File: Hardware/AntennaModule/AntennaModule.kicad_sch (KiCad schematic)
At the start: 0 parts

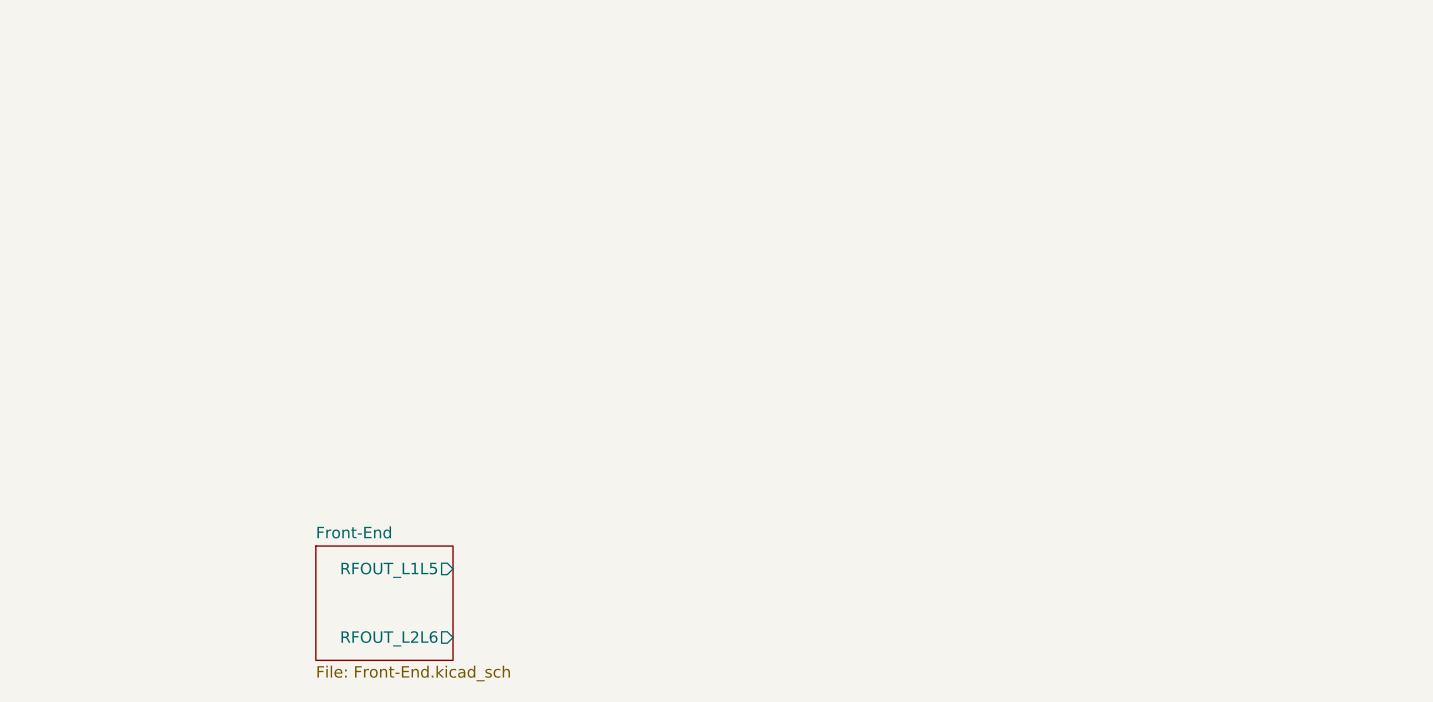
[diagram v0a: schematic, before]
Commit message: TE0149AをTE0133Bに変更
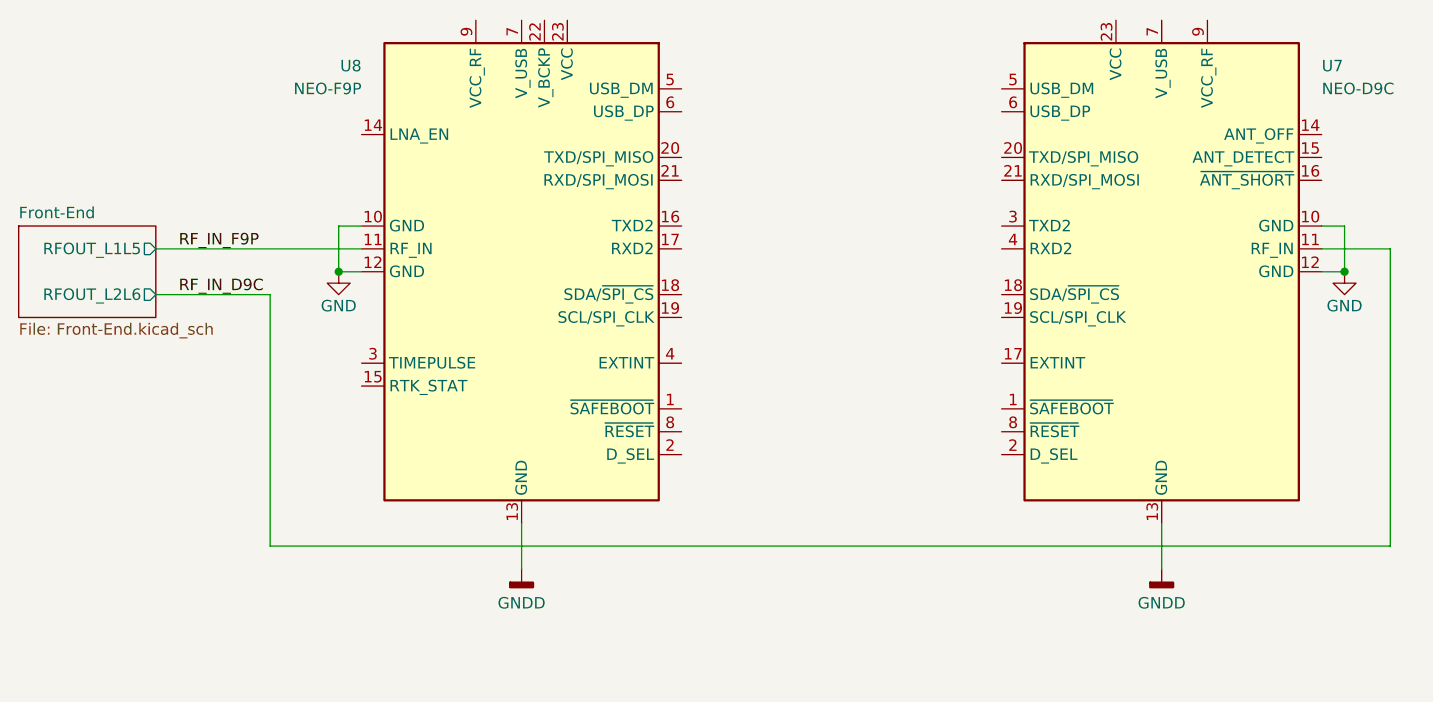
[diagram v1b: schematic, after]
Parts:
- added U7: NEO-D9C, RF_GPS:ublox_NEO, symbol RF_GNSS_extlib:NEO-D9C
- added U8: NEO-F9P, RF_GPS:ublox_NEO, symbol RF_GNSS_extlib:NEO-F9P
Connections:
- new net GND: U7.10 (GND), U7.12 (GND), U8.10 (GND), U8.12 (GND)
- new net GNDD: U7.13 (GND), U7.24 (GND), U8.13 (GND), U8.24 (GND)
- new net RF_IN_D9C: U7.11 (RF_IN)
- new net RF_IN_F9P: U8.11 (RF_IN)

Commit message: 回路図完成
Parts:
- added BT1: MS421R, Battery_extlib:Battery_Seiko_MS421R, symbol Device:Battery_Cell
- added C10: 2.2u, Capacitor_SMD:C_0603_1608Metric, symbol Device:C_Small
- added C11, C9: 1u, Capacitor_SMD:C_0603_1608Metric, symbol Device:C_Small
- added D1: CUHS20S30, Diode_SMD_extlib:D_Toshiba_US2H, symbol Device:D_Schottky_Small
- added D6: PULSE, symbol Device:LED_Small
- added J1: Conn_01x10, symbol Connector_Generic:Conn_01x10
- added R10, R4, R5, R6, R7, R9: 33, symbol Device:R_Small
- added R11: 1k, symbol Device:R_Small
- added R8: 3.3k, symbol Device:R_Small
- added SW1: ColdStart, Button_Switch_SMD:SW_Push_1P1T_NO_Vertical_Wuerth_434133025816, symbol Switch:SW_Push
- added TP1: ~{SAFEBOOT_F9P}, TestPoint:TestPoint_Pad_D1.0mm, symbol Connector:TestPoint_Small
- added TP2: ~{SAFEBOOT_D9C}, TestPoint:TestPoint_Pad_D1.0mm, symbol Connector:TestPoint_Small
- added TP3: EXTINT_F9P, TestPoint:TestPoint_Pad_D1.0mm, symbol Connector:TestPoint_Small
- added TP4: EXTINT_D9C, TestPoint:TestPoint_Pad_D1.0mm, symbol Connector:TestPoint_Small
- added TP5: LNA_EN, TestPoint:TestPoint_Pad_D1.0mm, symbol Connector:TestPoint_Small
- U7, U8: footprint RF_GPS:ublox_NEO -> RF_GNSS_extlib:ublox_NEO
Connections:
- net GNDD: now also U7.7 (V_USB), U8.7 (V_USB), BT1.2 (-), C10.2, C11.2, C9.2, D6.1 (K), J1.1 (Pin_1), SW1.1
- net at U7.1 (~{SAFEBOOT}): now also TP2.1
- net at U7.17 (EXTINT): now also TP4.1
- net at U7.18 (SDA/~{SPI_CS}): now also R10.2
- net SCL: now reaches U7.19 (SCL/SPI_CLK)
- net SCL: now also U8.19 (SCL/SPI_CLK), J1.4 (Pin_4)
- net at U7.20 (TXD/SPI_MISO): now also R7.2
- net RXD1_D9C: now reaches U7.21 (RXD/SPI_MOSI)
- net RXD1_D9C: now also J1.8 (Pin_8)
- net +3.3V: now reaches U7.23 (VCC)
- net +3.3V: now also U8.23 (VCC), C11.1, C9.1, D1.2 (A), J1.2 (Pin_2)
- net at U7.3 (TXD2): now also R5.2
- net at U7.4 (RXD2): now also R4.2
- net ~{RESET}: now reaches U7.8 (~{RESET})
- net ~{RESET}: now also U8.8 (~{RESET}), SW1.2
- net at U8.1 (~{SAFEBOOT}): now also TP1.1
- net at U8.14 (LNA_EN): now also TP5.1
- net RTK: now reaches U8.15 (RTK_STAT)
- net RTK: now also J1.10 (Pin_10)
- net at U8.16 (TXD2): now also R4.1
- net at U8.17 (RXD2): now also R5.1
- net at U8.18 (SDA/~{SPI_CS}): now also R9.1
- net at U8.20 (TXD/SPI_MISO): now also R6.1
- net RXD1_F9P: now reaches U8.21 (RXD/SPI_MOSI)
- net RXD1_F9P: now also J1.6 (Pin_6)
- net +BATT: now reaches U8.22 (V_BCKP)
- net +BATT: now also BT1.1 (+), C10.1, R8.2
- net TP: now reaches U8.3 (TIMEPULSE)
- net TP: now also J1.9 (Pin_9), R11.1
- net at U8.4 (EXTINT): now also TP3.1
- net +3.3VA: now reaches U8.9 (VCC_RF)
- new net: D1.1 (K), R8.1
- new net: D6.2 (A), R11.2
- new net SDA: J1.3 (Pin_3), R10.1, R9.2
- new net TXD1_D9C: J1.7 (Pin_7), R7.1
- new net TXD1_F9P: J1.5 (Pin_5), R6.2
- no-connect marks 0 -> 7
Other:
- note added: "10pinに収めて2x05ピンヘッダを使うのはあり"
- note added: "I2C peripheral mode only"
- note added: "I2C+UART only"
- note added: "LEDは果たして必要なのか"
- note added: "RESETはプルアップ抵抗内臓 UARTとかのIOからもコールドスタートさせられるのでRESETはコネクタに引き出さない D_SELはOPENでUART+I2C"
- note added: "SDA,SCLを共通にすると、SPI_CSとSPI_CLKも共通になる。 ペリフェラルのCSが共通の時点でSPIはまともに使えない よってD_SELはOPENで固定"
- note added: "ダンピング抵抗が必要か要らないかは、 sparkfun基板の特性Zと抵抗値から出力Zを見積もって決める 4層基板にすると同じ配線幅でも2層基板より特性Zが低くなり、ダンピング抵抗の値が小さくなる あんまり変わらん説はある"
- note added: "電流制限抵抗は電圧リップルの原因になりうるかも コネクタは無いのでオミットする？ LNA電源はF9PとD9Cのどちらかから取る LNAごとに変えても良いかも LNAごとに変えるなら+3.3VADCとか使う？ 3つのLNAにLNA_ENをつなげると経路設計が大変になるので使わない"
- moved on the sheet: U8

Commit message: アンテナの給電点が逆になっていたのを修正
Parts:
- D6: footprint (none) -> LED_SMD:LED_0402_1005Metric
- J1: footprint (none) -> Connector_PinHeader_1.27mm:PinHeader_2x05_P1.27mm_Vertical_SMD
- R10, R11, R4, R5, R6, R7, R8, R9: footprint (none) -> Resistor_SMD:R_0402_1005Metric
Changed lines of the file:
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@@
 			)
 		)
-		(property "Footprint" ""
+		(property "Footprint" "Resistor_SMD:R_0402_1005Metric"
 			(at 129.54 99.06 0)
 			(effects
@@
 			)
 		)
-		(property "Footprint" ""
+		(property "Footprint" "Resistor_SMD:R_0402_1005Metric"
 			(at 93.98 91.44 0)
 			(effects
@@
 			)
 		)
-		(property "Footprint" ""
+		(property "Footprint" "Resistor_SMD:R_0402_1005Metric"
 			(at 129.54 91.44 0)
 			(effects
@@
 			)
 		)
-		(property "Footprint" ""
+		(property "Footprint" "Resistor_SMD:R_0402_1005Metric"
 			(at 93.98 99.06 0)
 			(effects
@@
 			)
 		)
-		(property "Footprint" ""
+		(property "Footprint" "Resistor_SMD:R_0402_1005Metric"
 			(at 114.3 60.96 0)
 			(effects
@@
 			)
 		)
-		(property "Footprint" ""
+		(property "Footprint" "Resistor_SMD:R_0402_1005Metric"
 			(at 93.98 83.82 0)
 			(effects
@@
 			)
 		)
-		(property "Footprint" ""
+		(property "Footprint" "Resistor_SMD:R_0402_1005Metric"
 			(at 124.46 152.4 0)
 			(effects
@@
 			)
 		)
-		(property "Footprint" ""
+		(property "Footprint" "Connector_PinHeader_1.27mm:PinHeader_2x05_P1.27mm_Vertical_SMD"
 			(at 157.48 154.94 0)
 			(effects
@@
 			)
 		)
-		(property "Footprint" ""
+		(property "Footprint" "LED_SMD:LED_0402_1005Metric"
 			(at 124.46 157.48 90)
 			(effects
@@
 			)
 		)
-		(property "Footprint" ""
+		(property "Footprint" "Resistor_SMD:R_0402_1005Metric"
 			(at 129.54 83.82 0)
 			(effects

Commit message: スタックアップを決定
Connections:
- net +3.3VA: now also U7.9 (VCC_RF); no longer U8.9 (VCC_RF)
- new net +3.3VP: U8.9 (VCC_RF)
- no-connect marks 7 -> 6
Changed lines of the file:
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@@
 	)
 	(no_connect
-		(at 154.94 68.58)
-	)
-	(no_connect
 		(at 132.08 116.84)
 	)
@@
 	(wire
 		(pts
+			(xy 167.64 68.58) (xy 154.94 68.58)
+		)
+		(stroke
+			(width 0)
+			(type default)
+		)
+	)
+	(wire
+		(pts
 			(xy 127 91.44) (xy 111.76 91.44)
 		)
@@
 	)
 	(symbol
+		(lib_id "power:+3.3VP")
+		(at 55.88 68.58 90)
+		(unit 1)
+		(exclude_from_sim no)
+		(in_bom yes)
+		(on_board yes)
+		(dnp no)
+		(property "Reference" "#PWR047"
+			(at 57.15 64.77 0)
+			(effects
+				(font
+					(size 1.27 1.27)
+				)
+				(hide yes)
+			)
+		)
+		(property "Value" "+3.3VP"
+			(at 53.34 68.58 90)
+			(effects
+				(font
+					(size 1.27 1.27)
+				)
+				(justify left)
+			)
+		)
+		(property "Footprint" ""
+			(at 55.88 68.58 0)
+			(effects
+				(font
+					(size 1.27 1.27)
+				)
+				(hide yes)
+			)
+		)
+		(property "Datasheet" ""
+			(at 55.88 68.58 0)
+			(effects
+				(font
+					(size 1.27 1.27)
+				)
+				(hide yes)
+			)
+		)
+		(property "Description" "Power symbol creates a global label with name \"+3.3VP\""
+			(at 55.88 68.58 0)
+			(effects
+				(font
+					(size 1.27 1.27)
+				)
+				(hide yes)
+			)
+		)
+		(pin "1"
+		)
+		(instances
+			(project ""
+				(path "/6fea4726-6625-4d37-9d0c-c1a5d08d59ce"
+					(reference "#PWR047")
+					(unit 1)
+				)
+			)
+		)
+	)
+	(symbol
 		(lib_id "RF_GNSS_extlib:NEO-D9C")
 		(at 149.86 96.52 0)
@@
 	)
 	(symbol
-		(lib_id "power:+3.3VA")
-		(at 55.88 68.58 90)
-		(unit 1)
-		(exclude_from_sim no)
-		(in_bom yes)
-		(on_board yes)
-		(dnp no)
-		(property "Reference" "#PWR041"
-			(at 59.69 68.58 0)
-			(effects
-				(font
-					(size 1.27 1.27)
-				)
-				(hide yes)
-			)
-		)
-		(property "Value" "+3.3VA"
-			(at 53.34 68.58 90)
-			(effects
-				(font
-					(size 1.27 1.27)
-				)
-				(justify left)
-			)
-		)
-		(property "Footprint" ""
-			(at 55.88 68.58 0)
-			(effects
-				(font
-					(size 1.27 1.27)
-				)
-				(hide yes)
-			)
-		)
-		(property "Datasheet" ""
-			(at 55.88 68.58 0)
-			(effects
-				(font
-					(size 1.27 1.27)
-				)
-				(hide yes)
-			)
-		)
-		(property "Description" "Power symbol creates a global label with name \"+3.3VA\""
-			(at 55.88 68.58 0)
-			(effects
-				(font
-					(size 1.27 1.27)
-				)
-				(hide yes)
-			)
-		)
-		(pin "1"
-		)
-		(instances
-			(project ""
-				(path "/6fea4726-6625-4d37-9d0c-c1a5d08d59ce"
-					(reference "#PWR041")
-					(unit 1)
-				)
-			)
-		)
-	)
-	(symbol
 		(lib_id "Connector:TestPoint_Small")
 		(at 132.08 111.76 0)
@@
 					(unit 1)
 				)
+			)
+		)
+	)
+	(symbol
+		(lib_id "power:+3.3VA")
+		(at 167.64 68.58 270)
+		(mirror x)
+		(unit 1)
+		(exclude_from_sim no)
+		(in_bom yes)
+		(on_board yes)
+		(dnp no)
+		(property "Reference" "#PWR044"
+			(at 163.83 68.58 0)
+			(effects
+				(font
+					(size 1.27 1.27)
+				)
+				(hide yes)
+			)
+		)
+		(property "Value" "+3.3VA"
+			(at 170.18 68.58 90)
+			(effects
+				(font
+					(size 1.27 1.27)
+				)
+				(justify left)
+			)
+		)
+		(property "Footprint" ""
+			(at 167.64 68.58 0)
+			(effects
+				(font
+					(size 1.27 1.27)
+				)
+				(hide yes)
+			)
+		)
+		(property "Datasheet" ""
+			(at 167.64 68.58 0)
+			(effects
+				(font
+					(size 1.27 1.27)
+				)
+				(hide yes)
+			)
+		)
+		(property "Description" "Power symbol creates a global label with name \"+3.3VA\""
+			(at 167.64 68.58 0)
+			(effects
+				(font
+					(size 1.27 1.27)
+				)
+				(hide yes)
+			)
+		)
+		(pin "1"
+		)
+		(instances
+			(project "AntennaModule"
+				(path "/6fea4726-6625-4d37-9d0c-c1a5d08d59ce"
+					(reference "#PWR044")
+					(unit 1)
+				)
